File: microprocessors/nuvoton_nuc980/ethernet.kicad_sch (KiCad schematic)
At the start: 34 parts, among them J11 MTJ-88ARX1-LH, T1 SM13126PEL, U9 LAN8720A-CP, Y3 XTAL 25MHz 20pF

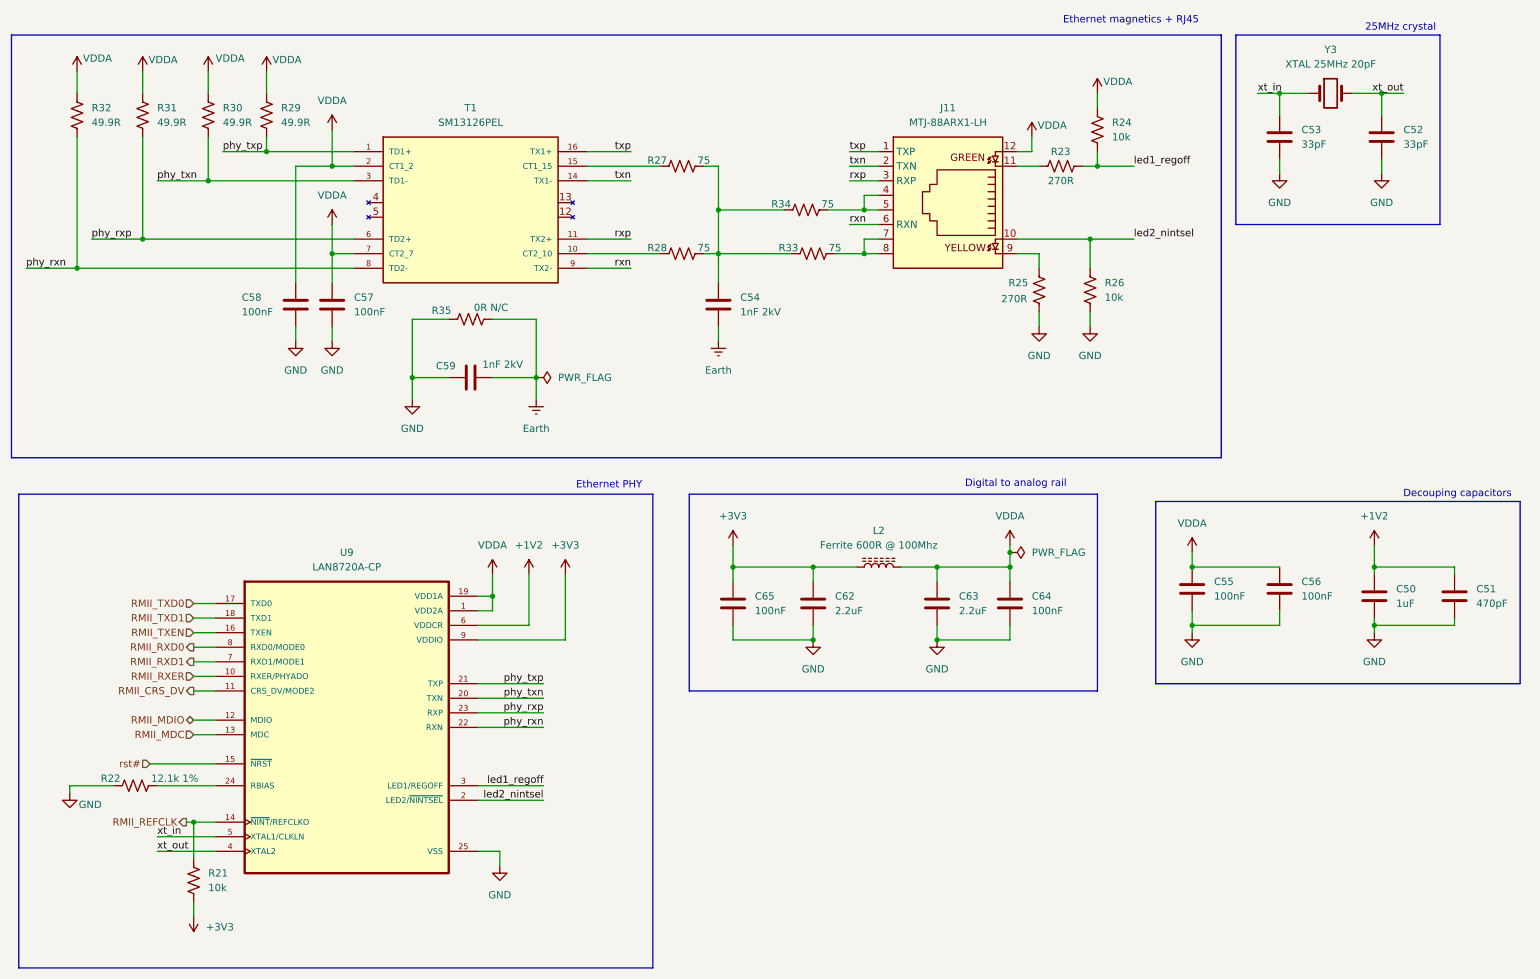
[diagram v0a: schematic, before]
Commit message: feat: ERC passing cotti-nuvoton
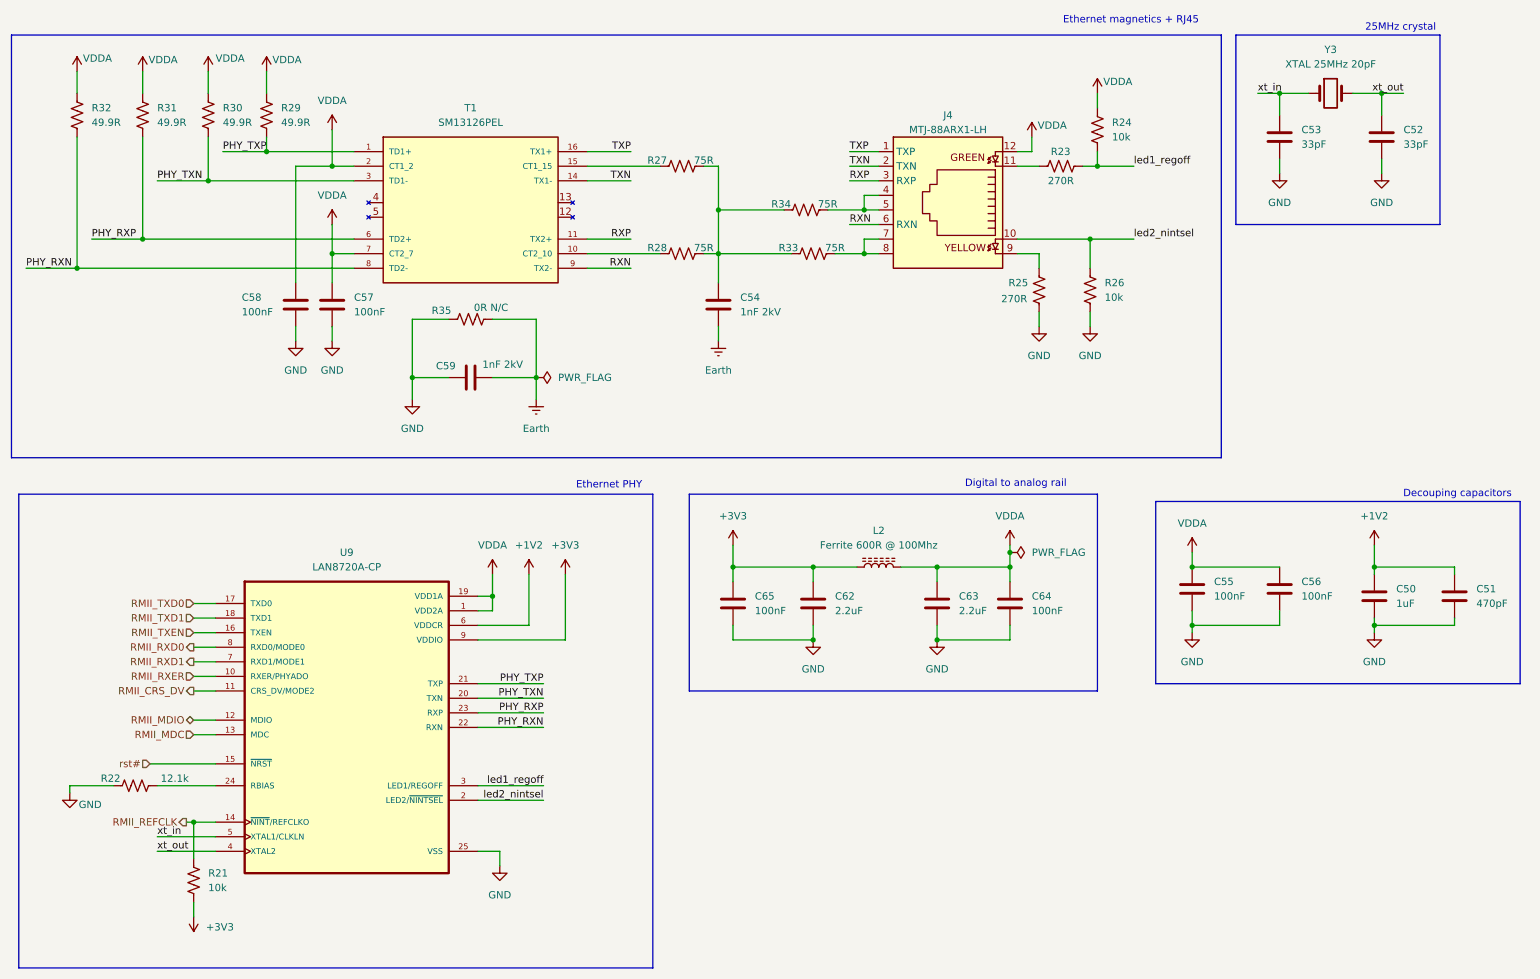
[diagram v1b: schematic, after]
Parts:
- removed J11: MTJ-88ARX1-LH, project_footprints:RJ45_MTJ-88ARX1-LH_ADM, symbol cotti_ethernet:RJ45_unshielded_leds
- added J4: MTJ-88ARX1-LH, cotti_footprints:RJ45_MTJ-88ARX1-LH_ADM, symbol cotti_ethernet:RJ45_unshielded_leds
- C50: footprint (none) -> Capacitor_SMD:C_0805_2012Metric_Pad1.18x1.45mm_HandSolder; Digikey (none) -> https://www.digikey.com/en/products/detail/samsung-electro-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; Mfr. (none) -> Samsung Electro-Mechanics; Mfr. P/N (none) -> CL21B105KBFNNNE
- C51: footprint (none) -> Capacitor_SMD:C_0805_2012Metric_Pad1.18x1.45mm_HandSolder; Digikey (none) -> https://www.digikey.com/en/products/detail/walsin-technolog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; Mfr. (none) -> Walsin Technology Corporation; Mfr. P/N (none) -> 0805B471K500CT
- C52, C53: footprint (none) -> Capacitor_SMD:C_0805_2012Metric_Pad1.18x1.45mm_HandSolder; Digikey (none) -> https://www.digikey.com/en/products/detail/yageo/CC0805JRNP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; Mfr. (none) -> YAGEO; Mfr. P/N (none) -> CC0805JRNPO9BN330
- C54, C59: footprint (none) -> Capacitor_SMD:C_1206_3216Metric_Pad1.33x1.80mm_HandSolder; Digikey (none) -> https://www.digikey.com/en/products/detail/walsin-technolog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; Mfr. (none) -> Walsin Technology Corporation; Mfr. P/N (none) -> 1206B102M202CT
- C55, C56, C57, C58, C64, C65: footprint (none) -> Capacitor_SMD:C_0805_2012Metric_Pad1.18x1.45mm_HandSolder; Digikey (none) -> https://www.digikey.com/en/products/detail/samsung-electro-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; Mfr. (none) -> Samsung Electro-Mechanics; Mfr. P/N (none) -> CL21B104KACNNNC
- C62, C63: footprint (none) -> Capacitor_SMD:C_0805_2012Metric_Pad1.18x1.45mm_HandSolder; Digikey (none) -> https://www.digikey.com/en/products/detail/cal-chip-electro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; Mfr. (none) -> Cal-Chip Electronics, Inc.; Mfr. P/N (none) -> GMC21X7R225K25NT
- L2: footprint (none) -> Inductor_SMD:L_0805_2012Metric_Pad1.05x1.20mm_HandSolder
- R21, R24, R26: footprint (none) -> Resistor_SMD:R_0805_2012Metric_Pad1.20x1.40mm_HandSolder; Digikey (none) -> https://www.digikey.com/en/products/detail/yageo/RC0805FR-1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; Mfr. (none) -> YAGEO; Mfr. P/N (none) -> RC0805FR-1310KL
- R22: value 12.1k 1% -> 12.1k; footprint (none) -> Resistor_SMD:R_0805_2012Metric_Pad1.20x1.40mm_HandSolder; Digikey (none) -> https://www.digikey.com/en/products/detail/yageo/AC0805FR-0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; Mfr. (none) -> YAGEO; Mfr. P/N (none) -> AC0805FR-0712K1L
- R23, R25: footprint (none) -> Resistor_SMD:R_0805_2012Metric_Pad1.20x1.40mm_HandSolder; Digikey (none) -> https://www.digikey.com/en/products/detail/yageo/RC0805FR-1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; Mfr. (none) -> YAGEO; Mfr. P/N (none) -> RC0805FR-10270RL
- R27, R28, R33, R34: value 75 -> 75R; footprint (none) -> Resistor_SMD:R_0805_2012Metric_Pad1.20x1.40mm_HandSolder; Digikey (none) -> https://www.digikey.com/en/products/detail/yageo/RC0805FR-1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; Mfr. (none) -> YAGEO; Mfr. P/N (none) -> RC0805FR-1375RL
- R29, R30, R31, R32: footprint (none) -> Resistor_SMD:R_0805_2012Metric_Pad1.20x1.40mm_HandSolder; Digikey (none) -> https://www.digikey.com/en/products/detail/yageo/RC0805FR-1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; Mfr. (none) -> YAGEO; Mfr. P/N (none) -> RC0805FR-1349R9L
- R35: footprint (none) -> Resistor_SMD:R_0805_2012Metric_Pad1.20x1.40mm_HandSolder; Digikey (none) -> https://www.digikey.com/en/products/detail/stackpole-electr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; Mfr. (none) -> Stackpole Electronics Inc; Mfr. P/N (none) -> RMCF0805ZG0R00
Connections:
- net VDDA: now also J4.12
- net led2_nintsel: now also J4.10
- net at R25.1: now also J4.9
- net at R23.2: now also J4.11
- net at R33.2: now also J4.7, J4.8
- net at R34.2: now also J4.4, J4.5
- net phy_rxn renamed PHY_RXN
- net phy_rxp renamed PHY_RXP
- net phy_txn renamed PHY_TXN
- net phy_txp renamed PHY_TXP
- net rxn renamed RXN
- net RXN: now also J4.6 (RXN)
- net rxp renamed RXP
- net RXP: now also J4.3 (RXP)
- net txn renamed TXN
- net TXN: now also J4.2 (TXN)
- net txp renamed TXP
- net TXP: now also J4.1 (TXP)
